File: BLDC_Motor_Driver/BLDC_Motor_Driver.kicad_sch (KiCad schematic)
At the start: 37 parts, among them J1 Conn_01x03_Socket, J101 Conn_02x12_Counter_Clockwise, J102 Conn_01x04, J2 Conn_01x05_Socket, J3 Conn_01x02, J4 USB4105-GF-A, J5 Conn_01x05, J7 Conn_01x05, SW1 SW_Push, SW2 SW_Push, U3 ECMF02-2AMX6

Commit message: schematics more or less done
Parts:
- removed J1: Conn_01x03_Socket, symbol Connector:Conn_01x03_Socket
- removed J2: Conn_01x05_Socket, symbol Connector:Conn_01x05_Socket
- added C103: 1uF, Capacitor_SMD:C_0603_1608Metric, symbol Device:C
- added J101: Conn_01x08, Connector_PinHeader_2.54mm:PinHeader_1x08_P2.54mm_Vertical, symbol Connector_Generic:Conn_01x08
- added J107, J110: 395221005, Connector_Molex_TerminalBlock:Molex_39522-005_1x05_P5.00mm_Horizontal, symbol Connector_Generic:Conn_01x05
- added J108: 395221003, Connector_Molex_TerminalBlock:Molex_39522-003_1x03_P5.00mm_Horizontal, symbol Connector_Generic:Conn_01x03
- added TP106: TestPoint, TestPoint:TestPoint_THTPad_D2.0mm_Drill1.0mm, symbol Connector:TestPoint
- J102: renamed from J3; value Conn_01x02 -> 395221002; footprint TerminalBlock_Phoenix:TerminalBlock_Phoenix_MKDS-1-2-3.81_1x02_P3.81mm_Horizontal -> Connector_Molex_TerminalBlock:Molex_39522-002_1x02_P5.00mm_Horizontal
- J103: renamed from J4; symbol Connector:USB_C_Receptacle_USB2.0 -> Connector:USB_C_Receptacle_USB2.0_16P
- J106: renamed from J102; footprint (none) -> Connector_PinHeader_2.54mm:PinHeader_1x04_P2.54mm_Vertical
- TP101, TP102, TP103, TP104, TP105: footprint (none) -> TestPoint:TestPoint_THTPad_D2.0mm_Drill1.0mm
- TP107: renamed from TP106; footprint (none) -> TestPoint:TestPoint_THTPad_D2.0mm_Drill1.0mm
- TP108: renamed from TP107; footprint (none) -> TestPoint:TestPoint_THTPad_D2.0mm_Drill1.0mm
- TP109: renamed from TP112; footprint (none) -> TestPoint:TestPoint_THTPad_D2.0mm_Drill1.0mm
- TP110: renamed from TP108; footprint (none) -> TestPoint:TestPoint_THTPad_D2.0mm_Drill1.0mm
- TP111: renamed from TP109; footprint (none) -> TestPoint:TestPoint_THTPad_D2.0mm_Drill1.0mm
- TP112: renamed from TP110; footprint (none) -> TestPoint:TestPoint_THTPad_D2.0mm_Drill1.0mm
- TP113: renamed from TP111; footprint (none) -> TestPoint:TestPoint_THTPad_D2.0mm_Drill1.0mm
- renumbered C113 to C101, C2 to C102, C1 to C104, D1 to D101, D2 to D102, D3 to D103, D4 to D104, J5 to J104, J7 to J105, J101 to J109, R14 to R101, R15 to R102, R16 to R103, R17 to R104, R12 to R105, R13 to R106, R11 to R107, SW2 to SW101, SW1 to SW102, U3 to U101
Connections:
- net SPI1_SCLK is gone; now on net SPI1_SCK: J109.20 (Pin_20)
- net SPI2_SCLK is gone; now on net SPI2_SCK: J105.2 (Pin_2)
- net 5V_DRV: now also C103.1, J107.1 (Pin_1), J110.1 (Pin_1)
- net D+: now also J103.A7 (D-), J103.B7 (D-); no longer J103.A6 (D+), J103.B6 (D+)
- net D-: now also J103.A6 (D+), J103.B6 (D+); no longer J103.A7 (D-), J103.B7 (D-)
- net GND: now also C103.2, J107.5 (Pin_5), J110.5 (Pin_5)
- net HALL_U_CONN: now also J107.2 (Pin_2)
- net HALL_V_CONN: now also J107.3 (Pin_3)
- net HALL_W_CONN: now also J107.4 (Pin_4)
- net MOTOR_U: now also J108.1 (Pin_1)
- net MOTOR_V: now also J108.2 (Pin_2)
- net MOTOR_W: now also J108.3 (Pin_3)
- new net DRIVER_WAKE: TP106.1
- new net ENC_A_CONN: J110.2 (Pin_2)
- new net ENC_B_CONN: J110.3 (Pin_3)
- new net ENC_N_CONN: J110.4 (Pin_4)
- new net Gate-Driver/ENC_A/TXEN: J101.1 (Pin_1)
- new net Gate-Driver/GPIO0: J101.2 (Pin_2)
- new net Gate-Driver/GPIO1: J101.3 (Pin_3)
- new net Gate-Driver/GPIO15: J101.5 (Pin_5)
- new net Gate-Driver/GPIO16: J101.6 (Pin_6)
- new net Gate-Driver/GPIO17: J101.7 (Pin_7)
- new net Gate-Driver/GPIO18: J101.8 (Pin_8)
- new net Gate-Driver/GPIO5: J101.4 (Pin_4)
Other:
- sheet Gate-Driver ports: added DRIVER_WAKE, ENC_A_CONN, ENC_A/TXEN, ENC_B_CONN, ENC_N_CONN, GPIO0, GPIO1, GPIO15, GPIO16, GPIO17, GPIO18, GPIO5; removed none
- sheet Microcontroller ports: added 3V3_REG; removed 3.3V_REG
- note added: "ENCODER CONNECTIONS AWG 26, MAX CURR <2A"
- note added: "HALL SENSE CONNECTIONS AWG 26, MAX CURR <2A"
- note added: "MOTOR PHASE CONNECTIONS AWG 20, MAX CURR 18A"
- note added: "change positions as needed to make routing easier"
- note added: "to driver"
- note removed: "AWG 20, MAX CURR <2A"
- note removed: "AWG 26, MAX CURR 18 A"
- note removed: "PHASE CONNECTIONS"
- note removed: "SENSE CONNECTIONS"
- note removed: "TODO: confirm that UART/SPI channels are necessary for normal operation"
- note removed: "TODO: finish HALL interface (depedent on finishing GPIO interface on 9660)"
- note removed: "TODO: map COMM channel(s) from uC to Gate Driver"
- note removed: "TODO: map uC pins to root"
- note removed: "to driver?"
- moved on the sheet: C101, C104, J104, SW102, TP107, TP108, TP109

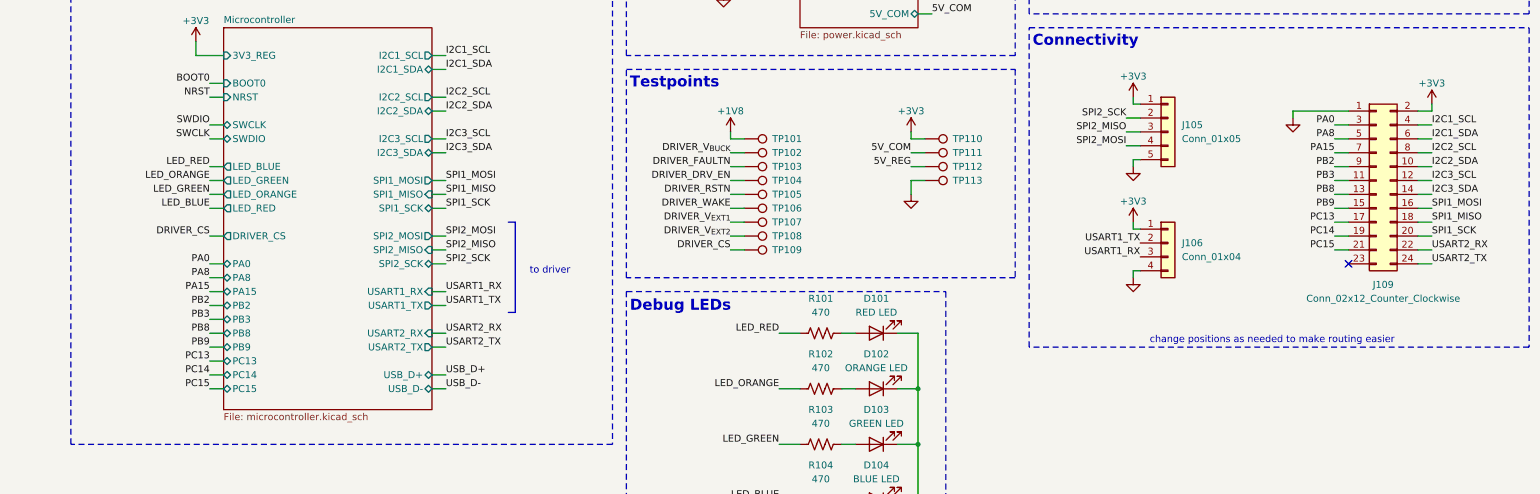
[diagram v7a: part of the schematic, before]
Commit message: wired driver rst/status ios to mcu, layout setup
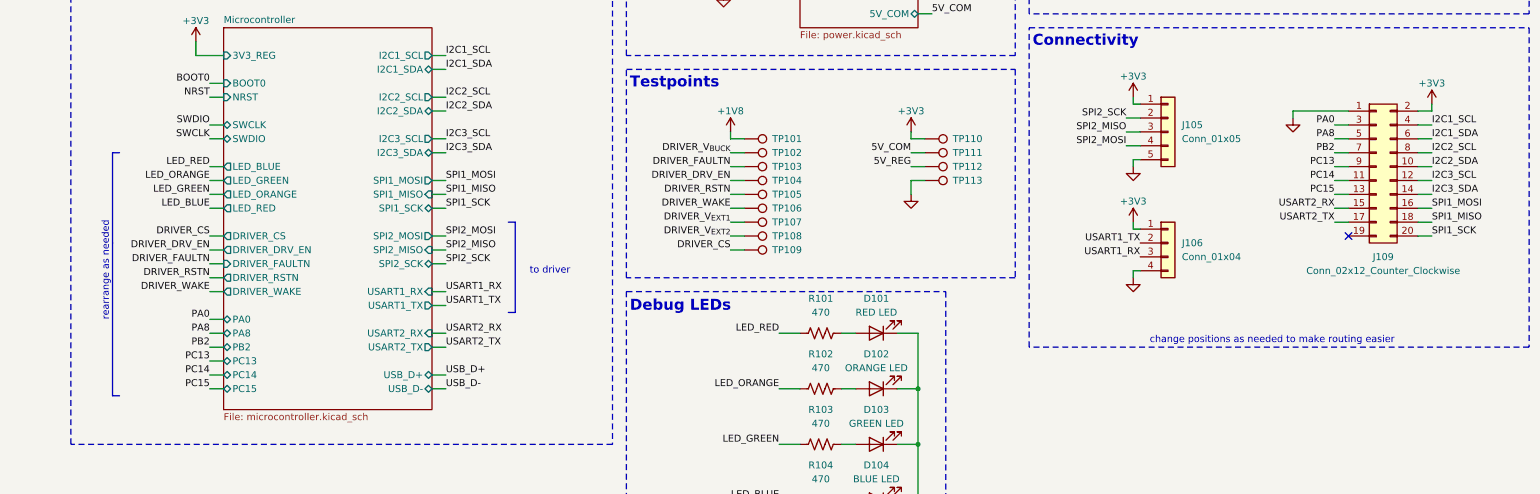
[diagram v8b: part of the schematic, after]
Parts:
- J109: footprint Connector_PinHeader_2.54mm:PinHeader_2x12_P2.54mm_Vertical -> Connector_PinHeader_2.54mm:PinHeader_2x10_P2.54mm_Vertical; symbol Connector_Generic:Conn_02x12_Odd_Even -> Connector_Generic:Conn_02x10_Odd_Even
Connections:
- net PA15 is gone; now on net PB2: J109.7 (Pin_7)
- net PB3 is gone; now on net PC14: J109.11 (Pin_11)
- net PB8 is gone; now on net PC15: J109.13 (Pin_13)
- net PB9 is gone; now on net USART2_RX: J109.15 (Pin_15)
- net PB2: no longer J109.9 (Pin_9)
- net PC13: now also J109.9 (Pin_9); no longer J109.17 (Pin_17)
- net PC14: no longer J109.19 (Pin_19)
- net PC15: no longer J109.21 (Pin_21)
- net USART2_RX: no longer J109.22 (Pin_22)
- net USART2_TX: now also J109.17 (Pin_17); no longer J109.24 (Pin_24)
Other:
- sheet Microcontroller ports: added DRIVER_DRV_EN, DRIVER_FAULTN, DRIVER_RSTN, DRIVER_WAKE; removed PA15, PB3, PB8, PB9
- note added: "rearrange as needed"
